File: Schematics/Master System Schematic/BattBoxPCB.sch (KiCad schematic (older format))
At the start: 16 parts

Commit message: LV Plate Cleanup + Other Small Stuff
> Renamed MCR PCB to BattBox PCB
> Added 7 Pin IMD connector to BattBox PCB
> Fixed wire gauges on Segment Layer sheet
> Added HV cutout on LV Plate
> Added fan signals
> Deleted old accumulator stuff
> Added BattBox and BMS fans

BattBox PCB V1.0
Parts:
- removed J?: IMD_PWR, symbol NER:2-Pos_Generic
- removed J?: MC_SIG, symbol NER:3-Pos_Generic
- added J?: 7-Pos_Generic, symbol NER:7-Pos_Generic
- added J?: 4-Pos_Generic, symbol NER:4-Pos_Generic
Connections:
- net CHRG_12V: now also J?.3
- net GND: now also J?.2
- net IMD_12V: now also J?.1
- net IMD_GND: now also J?.2
- net MC_AIR+: now also J?.2
- net MC_Precharge+: now also J?.1
- net at F?.1: now also J?.1
- new net: J?.1, J?.1, J?.1
- new net: J?.2, J?.2, J?.2
- new net IMD_Fault_IN: J?.3
- new net IMD_Fault_OUT: J?.4
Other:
- moved on the sheet: J?
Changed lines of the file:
@@
 $Descr A4 11693 8268
 encoding utf-8
-Sheet 18 40
-Title ""
-Date ""
-Rev ""
+Sheet 19 27
+Title "BattBox PCB"
+Date "2021-04-20"
+Rev "1.0"
 Comp ""
 Comment1 ""
@@
 L NER:2-Pos_Generic J?
 U 1 1 60881D3A
-P 8950 3750
-F 0 "J?" H 8950 3875 50  0000 C CNN
-F 1 "AIR+" H 8950 3784 50  0000 C CNN
-F 2 "" H 8950 3750 50  0001 C CNN
-F 3 "" H 8950 3750 50  0001 C CNN
-	1    8950 3750
+P 5600 5200
+F 0 "J?" H 5600 5325 50  0000 C CNN
+F 1 "AIR+" H 5600 5234 50  0000 C CNN
+F 2 "" H 5600 5200 50  0001 C CNN
+F 3 "" H 5600 5200 50  0001 C CNN
+	1    5600 5200
 	-1   0    0    -1
 $EndComp
@@
 L NER:2-Pos_Generic J?
 U 1 1 60883B2A
-P 8950 4300
-F 0 "J?" H 8950 4425 50  0000 C CNN
-F 1 "AIR-" H 8950 4334 50  0000 C CNN
-F 2 "" H 8950 4300 50  0001 C CNN
-F 3 "" H 8950 4300 50  0001 C CNN
-	1    8950 4300
+P 5600 5750
+F 0 "J?" H 5600 5875 50  0000 C CNN
+F 1 "AIR-" H 5600 5784 50  0000 C CNN
+F 2 "" H 5600 5750 50  0001 C CNN
+F 3 "" H 5600 5750 50  0001 C CNN
+	1    5600 5750
 	-1   0    0    -1
 $EndComp
@@
 L NER:2-Pos_Generic J?
 U 1 1 60883FAA
-P 8950 4850
-F 0 "J?" H 8950 4975 50  0000 C CNN
-F 1 "DCharge" H 8950 4884 50  0000 C CNN
-F 2 "" H 8950 4850 50  0001 C CNN
-F 3 "" H 8950 4850 50  0001 C CNN
-	1    8950 4850
+P 5600 6300
+F 0 "J?" H 5600 6425 50  0000 C CNN
+F 1 "DCharge" H 5600 6334 50  0000 C CNN
+F 2 "" H 5600 6300 50  0001 C CNN
+F 3 "" H 5600 6300 50  0001 C CNN
+	1    5600 6300
 	-1   0    0    -1
 $EndComp
@@
 L NER:2-Pos_Generic J?
 U 1 1 60884497
-P 8950 5400
-F 0 "J?" H 8950 5525 50  0000 C CNN
-F 1 "PCharge" H 8950 5434 50  0000 C CNN
-F 2 "" H 8950 5400 50  0001 C CNN
-F 3 "" H 8950 5400 50  0001 C CNN
-	1    8950 5400
+P 5600 6850
+F 0 "J?" H 5600 6975 50  0000 C CNN
+F 1 "PCharge" H 5600 6884 50  0000 C CNN
+F 2 "" H 5600 6850 50  0001 C CNN
+F 3 "" H 5600 6850 50  0001 C CNN
+	1    5600 6850
 	-1   0    0    -1
 $EndComp
-Text HLabel 9200 3850 2    50   Input ~ 0
+Text HLabel 5850 5300 2    50   Input ~ 0
 AIR+_SigH
-Text HLabel 9200 3950 2    50   Input ~ 0
+Text HLabel 5850 5400 2    50   Input ~ 0
 AIR+_SigL
-Text HLabel 9200 4400 2    50   Input ~ 0
+Text HLabel 5850 5850 2    50   Input ~ 0
 AIR-_SigH
-Text HLabel 9200 4500 2    50   Input ~ 0
+Text HLabel 5850 5950 2    50   Input ~ 0
 AIR-_SigL
-Text HLabel 9200 4950 2    50   Input ~ 0
+Text HLabel 5850 6400 2    50   Input ~ 0
 DCharge-_SigH
-Text HLabel 9200 5050 2    50   Input ~ 0
+Text HLabel 5850 6500 2    50   Input ~ 0
 DCharge-_SigL
-Text HLabel 9200 5500 2    50   Input ~ 0
+Text HLabel 5850 6950 2    50   Input ~ 0
 PCharge-_SigH
-Text HLabel 9200 5600 2    50   Input ~ 0
+Text HLabel 5850 7050 2    50   Input ~ 0
 PCharge-_SigL
 $Comp
@@
 F 3 "" H 8950 2250 50  0001 C CNN
 	1    8950 2250
-	1    0    0    -1
-$EndComp
-$Comp
-L NER:2-Pos_Generic J?
-U 1 1 6088A8C0
-P 8950 2850
-F 0 "J?" H 8950 2975 50  0000 C CNN
-F 1 "IMD_PWR" H 8950 2884 50  0000 C CNN
-F 2 "" H 8950 2850 50  0001 C CNN
-F 3 "" H 8950 2850 50  0001 C CNN
-	1    8950 2850
 	1    0    0    -1
 $EndComp
@@
 L NER:3-Pos_Generic J?
 U 1 1 608A0369
-P 2150 3750
-F 0 "J?" H 2150 3875 50  0000 C CNN
-F 1 "THERM_CAN" H 2150 3784 50  0000 C CNN
-F 2 "" H 2150 3750 50  0001 C CNN
-F 3 "" H 2150 3750 50  0001 C CNN
-	1    2150 3750
+P 2150 4650
+F 0 "J?" H 2150 4775 50  0000 C CNN
+F 1 "THERM_CAN" H 2150 4684 50  0000 C CNN
+F 2 "" H 2150 4650 50  0001 C CNN
+F 3 "" H 2150 4650 50  0001 C CNN
+	1    2150 4650
 	1    0    0    -1
 $EndComp
@@
 L NER:3-Pos_Generic J?
 U 1 1 608A1290
-P 2150 4400
-F 0 "J?" H 2150 4525 50  0000 C CNN
-F 1 "BMS_CAN" H 2150 4434 50  0000 C CNN
-F 2 "" H 2150 4400 50  0001 C CNN
-F 3 "" H 2150 4400 50  0001 C CNN
-	1    2150 4400
+P 2150 5300
+F 0 "J?" H 2150 5425 50  0000 C CNN
+F 1 "BMS_CAN" H 2150 5334 50  0000 C CNN
+F 2 "" H 2150 5300 50  0001 C CNN
+F 3 "" H 2150 5300 50  0001 C CNN
+	1    2150 5300
 	1    0    0    -1
 $EndComp
@@
 L NER:3-Pos_Generic J?
 U 1 1 608A1AB1
-P 2150 3100
-F 0 "J?" H 2150 3225 50  0000 C CNN
-F 1 "MAIN_CAN" H 2150 3134 50  0000 C CNN
-F 2 "" H 2150 3100 50  0001 C CNN
-F 3 "" H 2150 3100 50  0001 C CNN
-	1    2150 3100
-	1    0    0    -1
-$EndComp
-Text HLabel 1900 3200 0    50   Input ~ 0
+P 2150 4000
+F 0 "J?" H 2150 4125 50  0000 C CNN
+F 1 "MAIN_CAN" H 2150 4034 50  0000 C CNN
+F 2 "" H 2150 4000 50  0001 C CNN
+F 3 "" H 2150 4000 50  0001 C CNN
+	1    2150 4000
+	1    0    0    -1
+$EndComp
+Text HLabel 1900 4100 0    50   Input ~ 0
 GLV_CANH
-Text HLabel 1900 3300 0    50   Input ~ 0
+Text HLabel 1900 4200 0    50   Input ~ 0
 GLV_CANL
-Text HLabel 1900 3400 0    50   Input ~ 0
+Text HLabel 1900 4300 0    50   Input ~ 0
 GLV_CANS
-Text HLabel 1900 3850 0    50   Input ~ 0
+Text HLabel 1900 4750 0    50   Input ~ 0
 THRM_CANH
-Text HLabel 1900 3950 0    50   Input ~ 0
+Text HLabel 1900 4850 0    50   Input ~ 0
 THRM_CANL
-Text HLabel 1900 4050 0    50   Input ~ 0
+Text HLabel 1900 4950 0    50   Input ~ 0
 THRM_CANS
-Text HLabel 1900 4500 0    50   Input ~ 0
+Text HLabel 1900 5400 0    50   Input ~ 0
 BMS_CANH
-Text HLabel 1900 4600 0    50   Input ~ 0
+Text HLabel 1900 5500 0    50   Input ~ 0
 BMS_CANL
-Text HLabel 1900 4700 0    50   Input ~ 0
+Text HLabel 1900 5600 0    50   Input ~ 0
 BMS_CANS
 Wire Wire Line
-	2400 3400 2550 3400
-Wire Wire Line
-	2550 3400 2550 4050
-Wire Wire Line
-	2400 4700 2550 4700
-Connection ~ 2550 4700
-Wire Wire Line
-	2550 4700 2550 4950
-Wire Wire Line
-	2400 4050 2550 4050
-Connection ~ 2550 4050
-Wire Wire Line
-	2550 4050 2550 4700
+	2400 4300 2550 4300
+Wire Wire Line
+	2550 4300 2550 4950
+Wire Wire Line
+	2400 5600 2550 5600
+Connection ~ 2550 5600
+Wire Wire Line
+	2550 5600 2550 5850
+Wire Wire Line
+	2400 4950 2550 4950
+Connection ~ 2550 4950
+Wire Wire Line
+	2550 4950 2550 5600
 $Comp
 L power:GND #PWR?
 U 1 1 608A5D0A
-P 2550 4950
-F 0 "#PWR?" H 2550 4700 50  0001 C CNN
-F 1 "GND" H 2555 4777 50  0000 C CNN
-F 2 "" H 2550 4950 50  0001 C CNN
-F 3 "" H 2550 4950 50  0001 C CNN
-	1    2550 4950
+P 2550 5850
+F 0 "#PWR?" H 2550 5600 50  0001 C CNN
+F 1 "GND" H 2555 5677 50  0000 C CNN
+F 2 "" H 2550 5850 50  0001 C CNN
+F 3 "" H 2550 5850 50  0001 C CNN
+	1    2550 5850
 	1    0    0    -1
 $EndComp
@@
 L power:GND #PWR?
 U 1 1 608A67E2
-P 8700 3050
-F 0 "#PWR?" H 8700 2800 50  0001 C CNN
-F 1 "GND" H 8705 2877 50  0000 C CNN
-F 2 "" H 8700 3050 50  0001 C CNN
-F 3 "" H 8700 3050 50  0001 C CNN
-	1    8700 3050
-	1    0    0    -1
-$EndComp
-Wire Wire Line
-	2400 3300 2650 3300
-Wire Wire Line
-	2650 3300 2650 3950
-Wire Wire Line
-	2650 3950 2400 3950
-Wire Wire Line
-	2650 3950 2650 4600
-Wire Wire Line
-	2650 4600 2400 4600
-Connection ~ 2650 3950
-Wire Wire Line
-	2400 3200 2750 3200
-Wire Wire Line
-	2750 3200 2750 3850
-Wire Wire Line
-	2750 3850 2400 3850
-Wire Wire Line
-	2750 3850 2750 4500
-Wire Wire Line
-	2750 4500 2400 4500
-Connection ~ 2750 3850
+P 8550 3050
+F 0 "#PWR?" H 8550 2800 50  0001 C CNN
+F 1 "GND" H 8555 2877 50  0000 C CNN
+F 2 "" H 8550 3050 50  0001 C CNN
+F 3 "" H 8550 3050 50  0001 C CNN
+	1    8550 3050
+	1    0    0    -1
+$EndComp
+Wire Wire Line
+	2400 4200 2650 4200
+Wire Wire Line
+	2650 4200 2650 4850
+Wire Wire Line
+	2650 4850 2400 4850
+Wire Wire Line
+	2650 4850 2650 5500
+Wire Wire Line
+	2650 5500 2400 5500
+Connection ~ 2650 4850
+Wire Wire Line
+	2400 4100 2750 4100
+Wire Wire Line
+	2750 4100 2750 4750
+Wire Wire Line
+	2750 4750 2400 4750
+Wire Wire Line
+	2750 4750 2750 5400
+Wire Wire Line
+	2750 5400 2400 5400
+Connection ~ 2750 4750
 $Comp
 L NER:3-Pos_Generic J?
@@
 	1    0    0    -1
 $EndComp
-$Comp
-L NER:3-Pos_Generic J?
-U 1 1 61825C1A
-P 2150 2300
-F 0 "J?" H 2150 2425 50  0000 C CNN
-F 1 "MC_SIG" H 2150 2334 50  0000 C CNN
-F 2 "" H 2150 2300 50  0001 C CNN
-F 3 "" H 2150 2300 50  0001 C CNN
-	1    2150 2300
-	1    0    0    -1
-$EndComp
 Text HLabel 1900 2400 0    50   Input ~ 0
 MC_Precharge+
@@
 Text HLabel 1900 2600 0    50   Input ~ 0
 CHRG_12V
+$Comp
+L NER:7-Pos_Generic J?
+U 1 1 608C6250
+P 8950 2850
+F 0 "J?" H 8950 2975 50  0000 C CNN
+F 1 "7-Pos_Generic" H 8950 2884 50  0000 C CNN
+F 2 "" H 8950 2850 50  0001 C CNN
+F 3 "" H 8950 2850 50  0001 C CNN
+	1    8950 2850
+	1    0    0    -1
+$EndComp
+Wire Wire Line
+	8550 3050 8700 3050
+Wire Wire Line
+	8550 2950 8700 2950
+Text HLabel 9200 3150 2    50   Input ~ 0
+IMD_Fault_IN
+$Comp
+L NER:4-Pos_Generic J?
+U 1 1 608E1079
+P 2150 2300
+F 0 "J?" H 2150 2425 50  0000 C CNN
+F 1 "4-Pos_Generic" H 2150 2334 50  0000 C CNN
+F 2 "" H 2150 2300 50  0001 C CNN
+F 3 "" H 2150 2300 50  0001 C CNN
+	1    2150 2300
+	1    0    0    -1
+$EndComp
+Text HLabel 1900 2700 0    50   Input ~ 0
+IMD_Fault_OUT
 $EndSCHEMATC

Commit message: Master Cleanup
> BattBox sheet tweaks
> Removed IMD container
> Removed BattBox fans from master
> Removed BMS container, temporarily moved VPM sheet
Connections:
- new net: J?.1, J?.1, J?.1
- new net: J?.2, J?.2, J?.2
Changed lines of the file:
@@
 $Descr A4 11693 8268
 encoding utf-8
-Sheet 19 27
+Sheet 19 25
 Title "BattBox PCB"
 Date "2021-04-20"

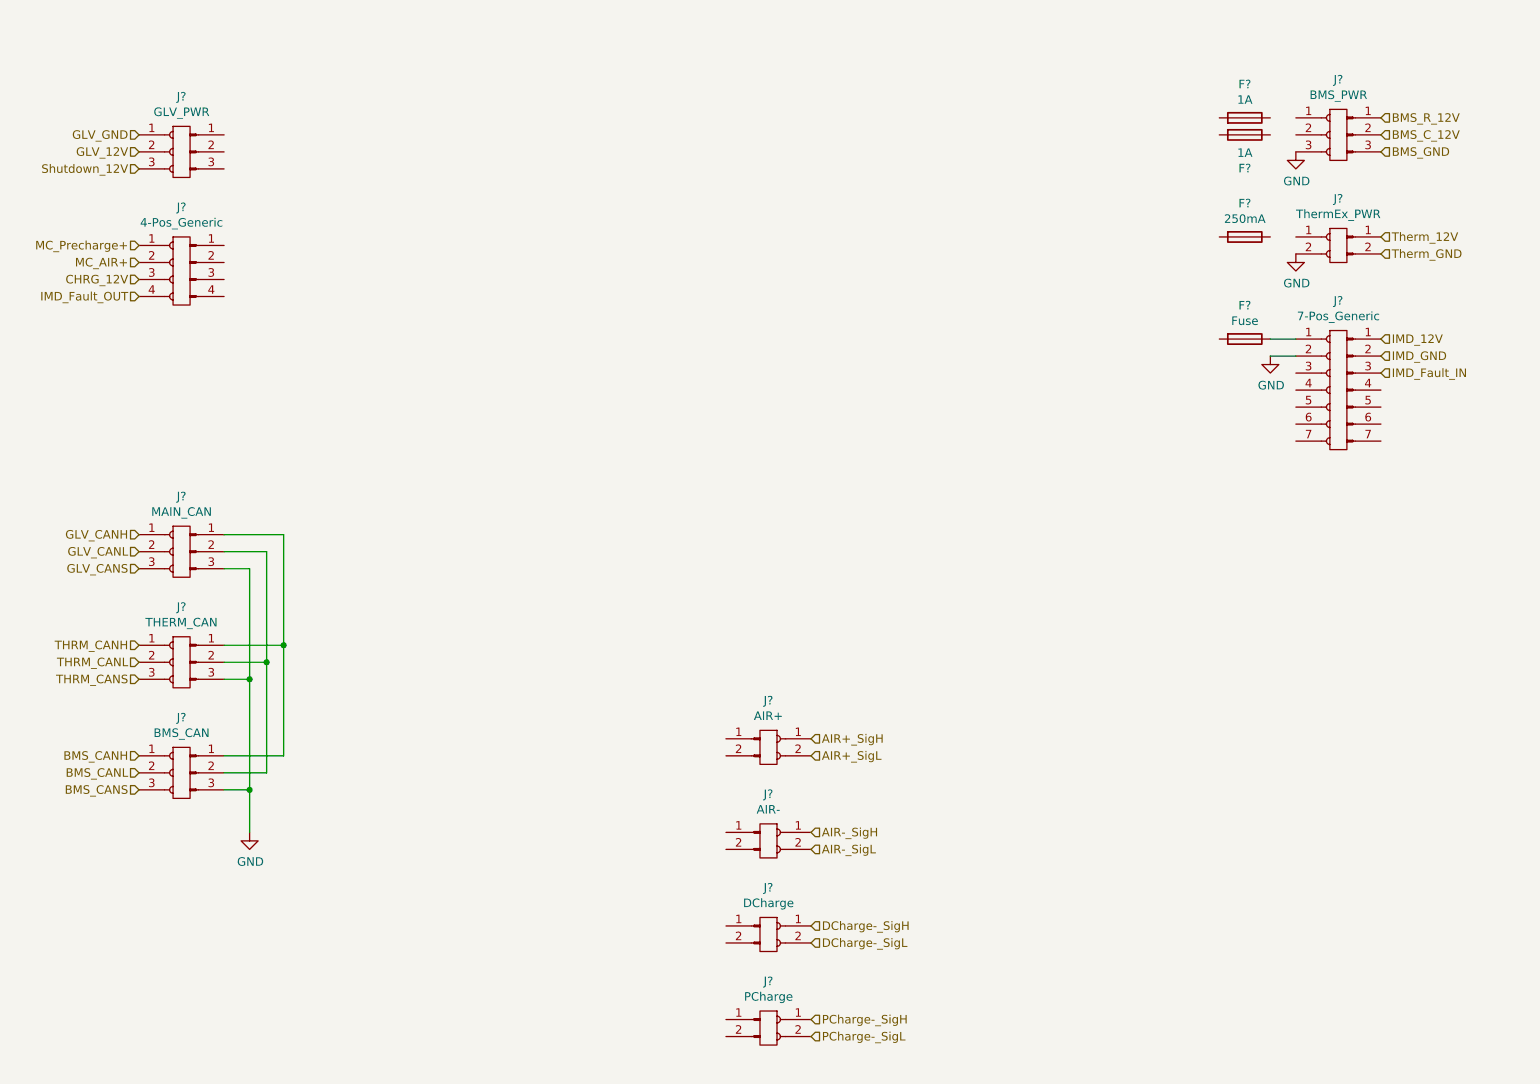
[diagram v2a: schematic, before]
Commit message: LV Plate and VPM board
Verified and updated LV plate connections
Setup VPM board stand-in
Organized main battery box schematic
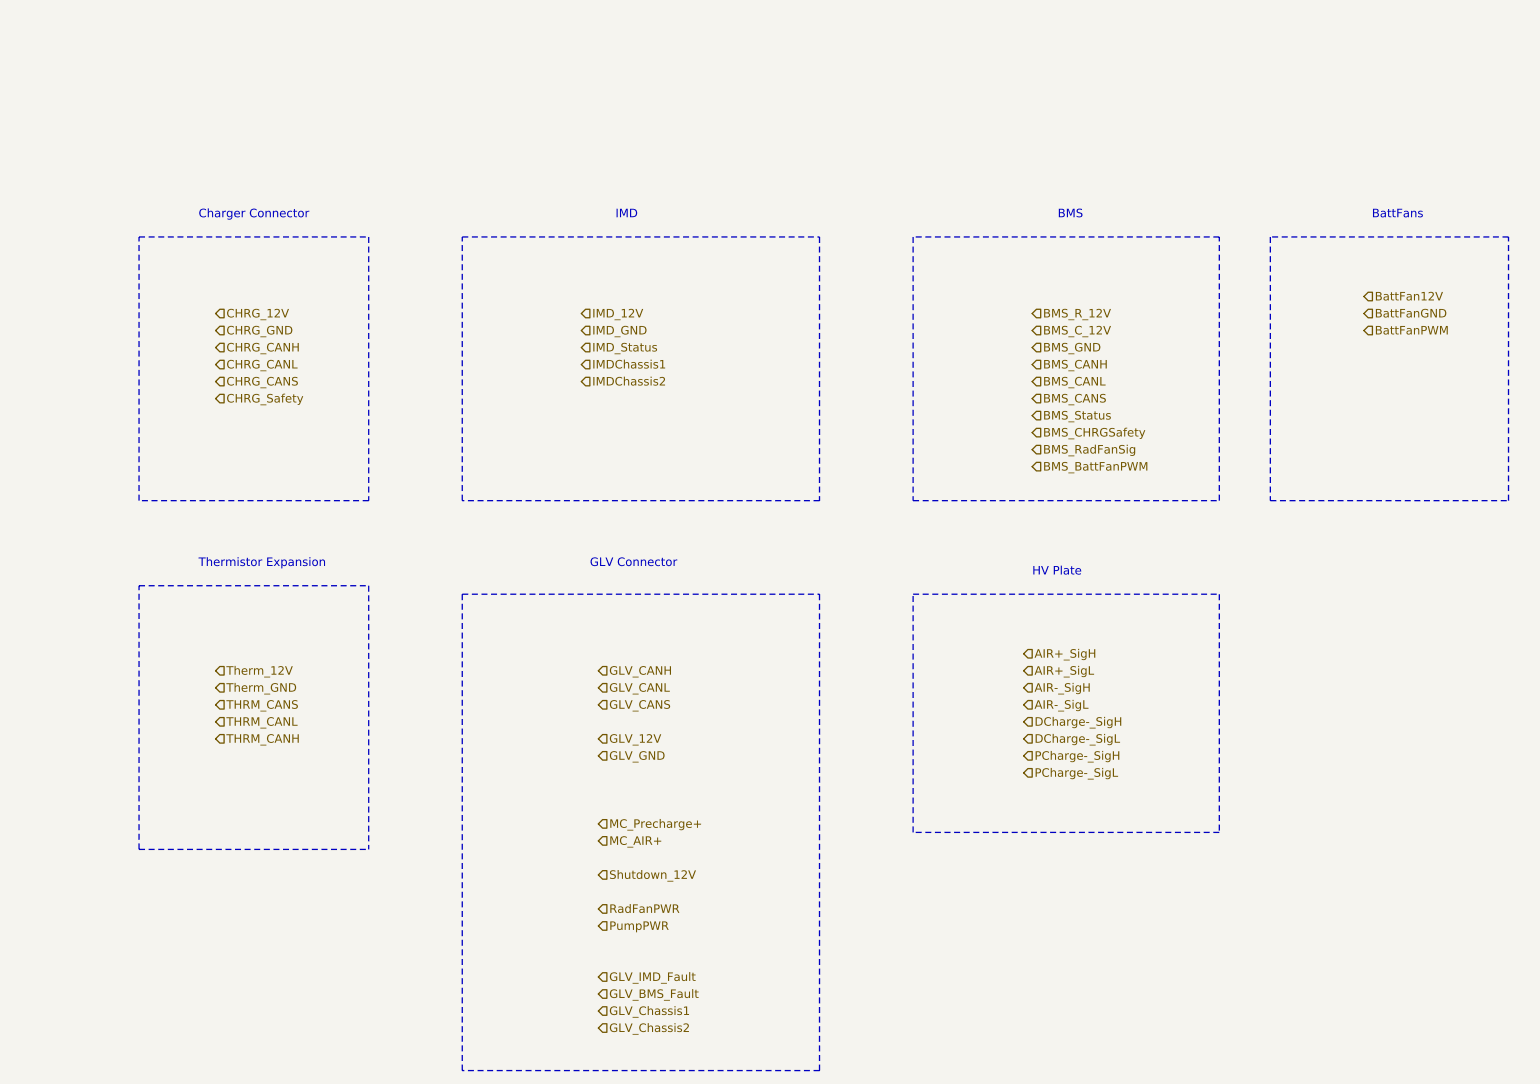
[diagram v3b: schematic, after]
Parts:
- removed F? (x2): 1A, symbol Device:Fuse
- removed F?: 250mA, symbol Device:Fuse
- removed F?: Fuse, symbol Device:Fuse
- removed J?: AIR+, symbol NER:2-Pos_Generic
- removed J?: AIR-, symbol NER:2-Pos_Generic
- removed J?: DCharge, symbol NER:2-Pos_Generic
- removed J?: PCharge, symbol NER:2-Pos_Generic
- removed J?: ThermEx_PWR, symbol NER:2-Pos_Generic
- removed J?: GLV_PWR, symbol NER:3-Pos_Generic
- removed J?: THERM_CAN, symbol NER:3-Pos_Generic
- removed J?: BMS_CAN, symbol NER:3-Pos_Generic
- removed J?: MAIN_CAN, symbol NER:3-Pos_Generic
- removed J?: BMS_PWR, symbol NER:3-Pos_Generic
- removed J?: 7-Pos_Generic, symbol NER:7-Pos_Generic
- removed J?: 4-Pos_Generic, symbol NER:4-Pos_Generic
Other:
- note added: "BMS"
- note added: "BattFans\n"
- note added: "Charger Connector"
- note added: "GLV Connector"
- note added: "HV Plate"
- note added: "IMD"
- note added: "Thermistor Expansion\n"

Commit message: VPM callout
Added call to view altium schematic for VPM boarrd
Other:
- note added: "SEE ALTIUM SCHEMATIC FOR FINAL IMPLEMENTATION"
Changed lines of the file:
@@
 Text HLabel 4600 5300 2    50   Input ~ 0
 GLV_12V
+Text Notes 2850 1300 0    157  ~ 0
+SEE ALTIUM SCHEMATIC FOR FINAL IMPLEMENTATION
 $EndSCHEMATC
